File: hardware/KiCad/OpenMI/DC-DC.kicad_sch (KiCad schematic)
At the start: 5 parts

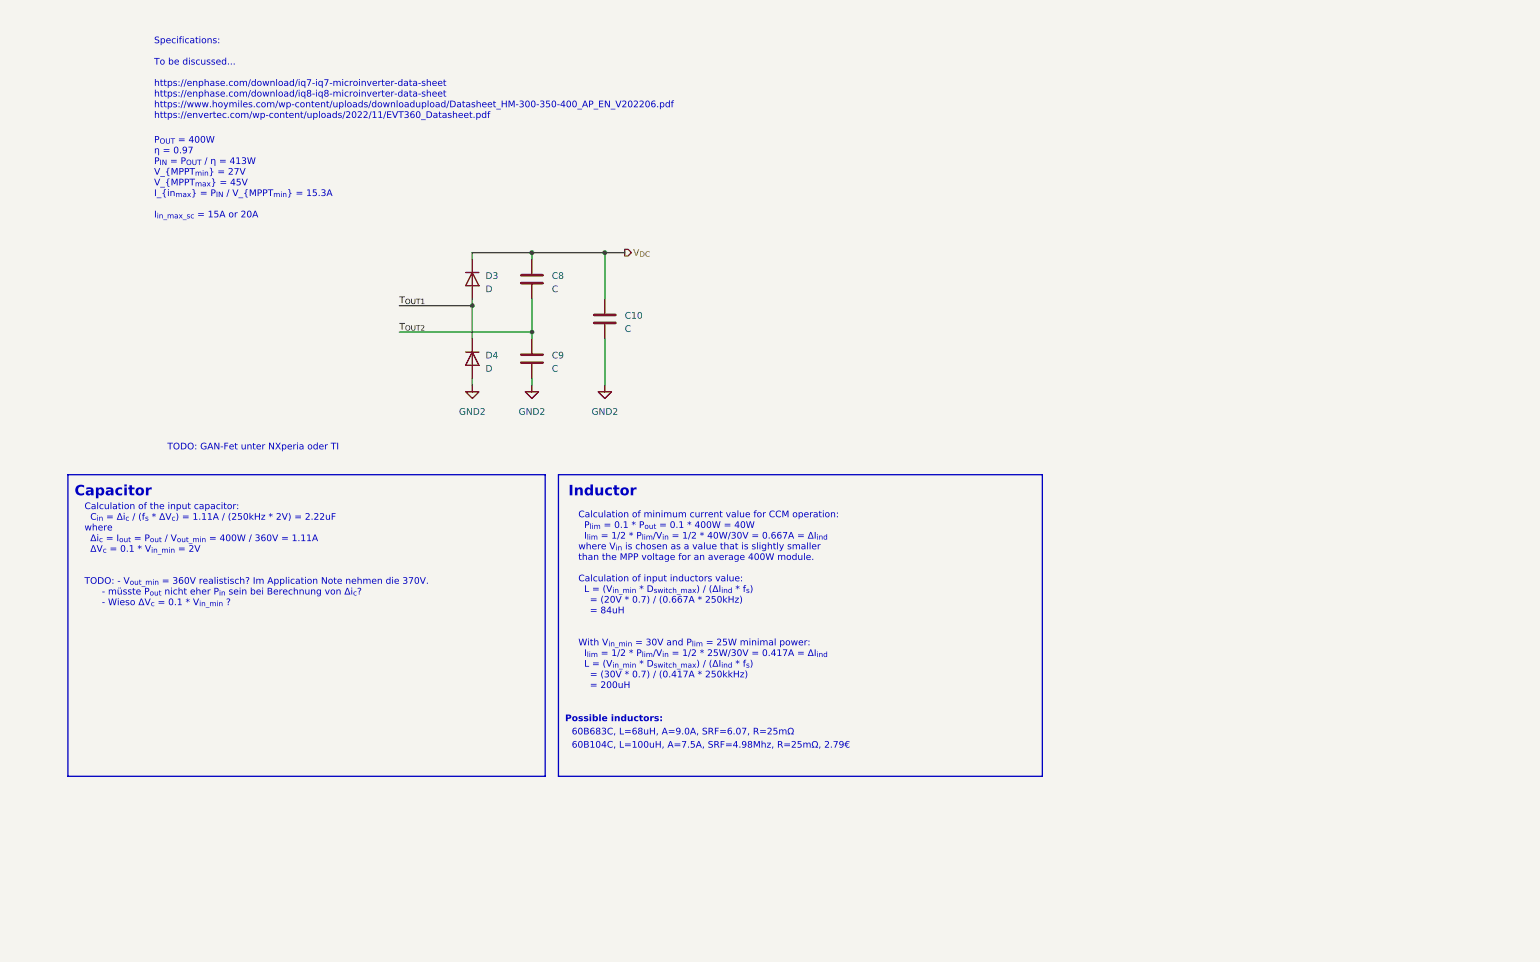
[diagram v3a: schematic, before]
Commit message: feat(hw): Add input capacitance and inductor suggestions
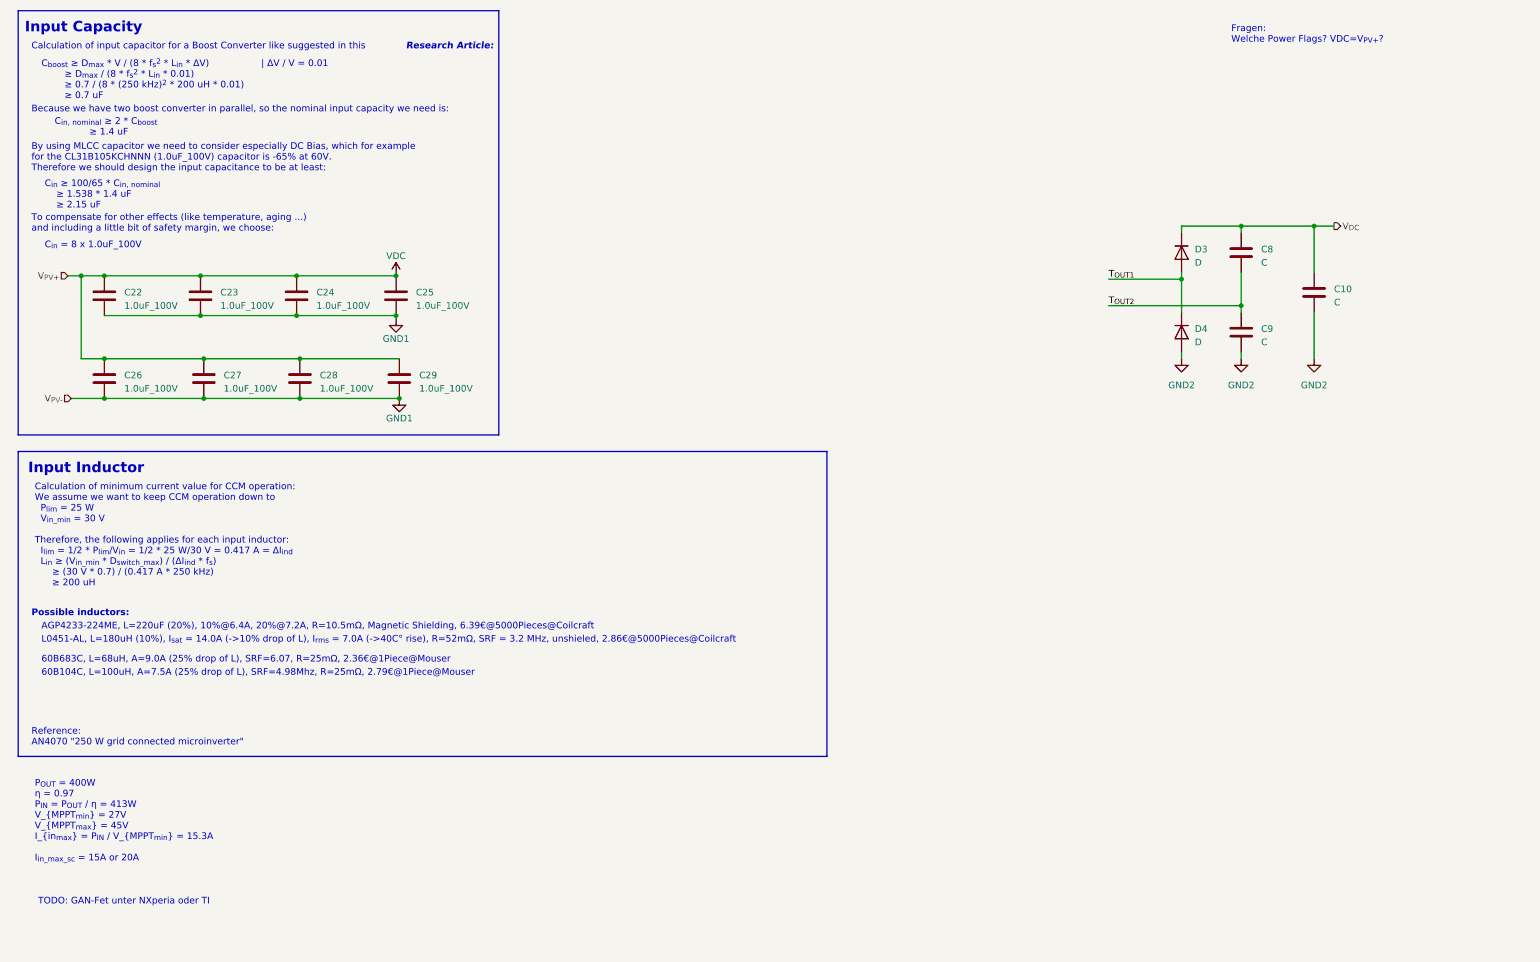
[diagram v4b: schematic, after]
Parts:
- added C22, C23, C24, C25, C26, C27, C28, C29: 1.0uF_100V, Capacitor_SMD:C_1206_3216Metric, symbol _C_1206:1.0uF_100V
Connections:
- new net GND1: C22.2, C23.2, C24.2, C25.2, C26.2, C27.2, C28.2, C29.2
- new net VDC: C22.1, C23.1, C24.1, C25.1, C26.1, C27.1, C28.1, C29.1
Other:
- note added: "60B104C, L=100uH, A=7.5A (25% drop of L), SRF=4.98Mhz, R=25mΩ, 2.79€@1Piece@Mouser"
- note added: "60B683C, L=68uH, A=9.0A (25% drop of L), SRF=6.07, R=25mΩ, 2.36€@1Piece@Mouser"
- note added: "AGP4233-224ME, L=220uF (20%), 10%@6.4A, 20%@7.2A, R=10.5mΩ, Magnetic Shielding, 6.39€@5000Pieces@Coilcraft"
- note added: "Because we have two boost converter in parallel, so the nominal input capacity we need is:"
- note added: "By using MLCC capacitor we need to consider especially DC Bias, which for example for the CL31B105KCHNNN (1.0uF_100V) capacitor is -65% at 60V. Therefore we should design the input capacitance to be at least:"
- note added: "C_{boost} ≥ D_{max} * V / (8 * f_{s}^{2} * L_{in} * ΔV) | ΔV / V = 0.01 ≥ D_{max} / (8 * f_{s}^{2} * L_{in} * 0.01) ≥ 0.7 / (8 * (250 kHz)^{2} * 200 uH * 0.01) ≥ 0.7 uF"
- note added: "C_{in, nominal} ≥ 2 * C_{boost} ≥ 1.4 uF"
- note added: "C_{in} = 8 x 1.0uF_100V"
- note added: "C_{in} ≥ 100/65 * C_{in, nominal} ≥ 1.538 * 1.4 uF ≥ 2.15 uF"
- note added: "Calculation of input capacitor for a Boost Converter like suggested in this"
- note added: "Calculation of minimum current value for CCM operation: We assume we want to keep CCM operation down to P_{lim} = 25 W V_{in_min} = 30 V Therefore, the following applies for each input inductor: I_{lim} = 1/2 * P_{lim}/V_{in} = 1/2 * 25 W/30 V = 0.417 A = ΔI_{ind} L_{in} ≥ (V_{in_min} * D_{switch_max}) / (ΔI_{ind} * f_{s}) ≥ (30 V * 0.7) / (0.417 A * 250 kHz) ≥ 200 uH"
- note added: "Fragen: Welche Power Flags? VDC=V_{PV+}?"
- note added: "Input Capacity"
- note added: "Input Inductor"
- note added: "L0451-AL, L=180uH (10%), I_{sat} = 14.0A (->10% drop of L), I_{rms} = 7.0A (->40C° rise), R=52mΩ, SRF = 3.2 MHz, unshieled, 2.86€@5000Pieces@Coilcraft"
- note added: "Reference: AN4070 "250 W grid connected microinverter""
- note added: "Research Article:"
- note added: "To compensate for other effects (like temperature, aging ...) and including a little bit of safety margin, we choose:"
- note removed: "60B104C, L=100uH, A=7.5A, SRF=4.98Mhz, R=25mΩ, 2.79€"
- note removed: "60B683C, L=68uH, A=9.0A, SRF=6.07, R=25mΩ"
- note removed: "Calculation of minimum current value for CCM operation: P_{lim} = 0.1 * P_{out} = 0.1 * 400W = 40W I_{lim} = 1/2 * P_{lim}/V_{in} = 1/2 * 40W/30V = 0.667A = ΔI_{ind} where V_{in} is chosen as a value that is slightly smaller than the MPP voltage for an average 400W module. Calculation of input inductors value: L = (V_{in_min} * D_{switch_max}) / (ΔI_{ind} * f_{s}) = (20V * 0.7) / (0.667A * 250kHz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"
- note removed: "Calculation of the input capacitor: C_{in} = Δi_{c} / (f_{s} * ΔV_{c}) = 1.11A / (250kHz * 2V) = 2.22uF where Δi_{c} = I_{out} = P_{out} / V_{out_min} = 400W / 360V = 1.11A ΔV_{c} = 0.1 * V_{in_min} = 2V TODO: - V_{out_min} = 360V realistisch? Im Application Note nehmen die 370V. - müsste P_{out} nicht eher P_{in} sein bei Berechnung von Δi_{c}? - Wieso ΔV_{c} = 0.1 * V_{in_min} ?"
- note removed: "Capacitor"
- note removed: "Inductor"
- note removed: "Specifications: To be discussed... https://enphase.com/download/iq7-iq7-microinverter-data-sheet https://enphase.com/download/iq8-iq8-microinverter-data-sheet https://www.hoymiles.com/wp-content/uploads/downloadupload/Datasheet_HM-300-350-400_AP_EN_V202206.pdf https://envertec.com/wp-content/uploads/2022/11/EVT360_Datasheet.pdf"
- moved on the sheet: C10, C8, C9, D3, D4

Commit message: docs(hw): Add first suggestions for GAN-FET
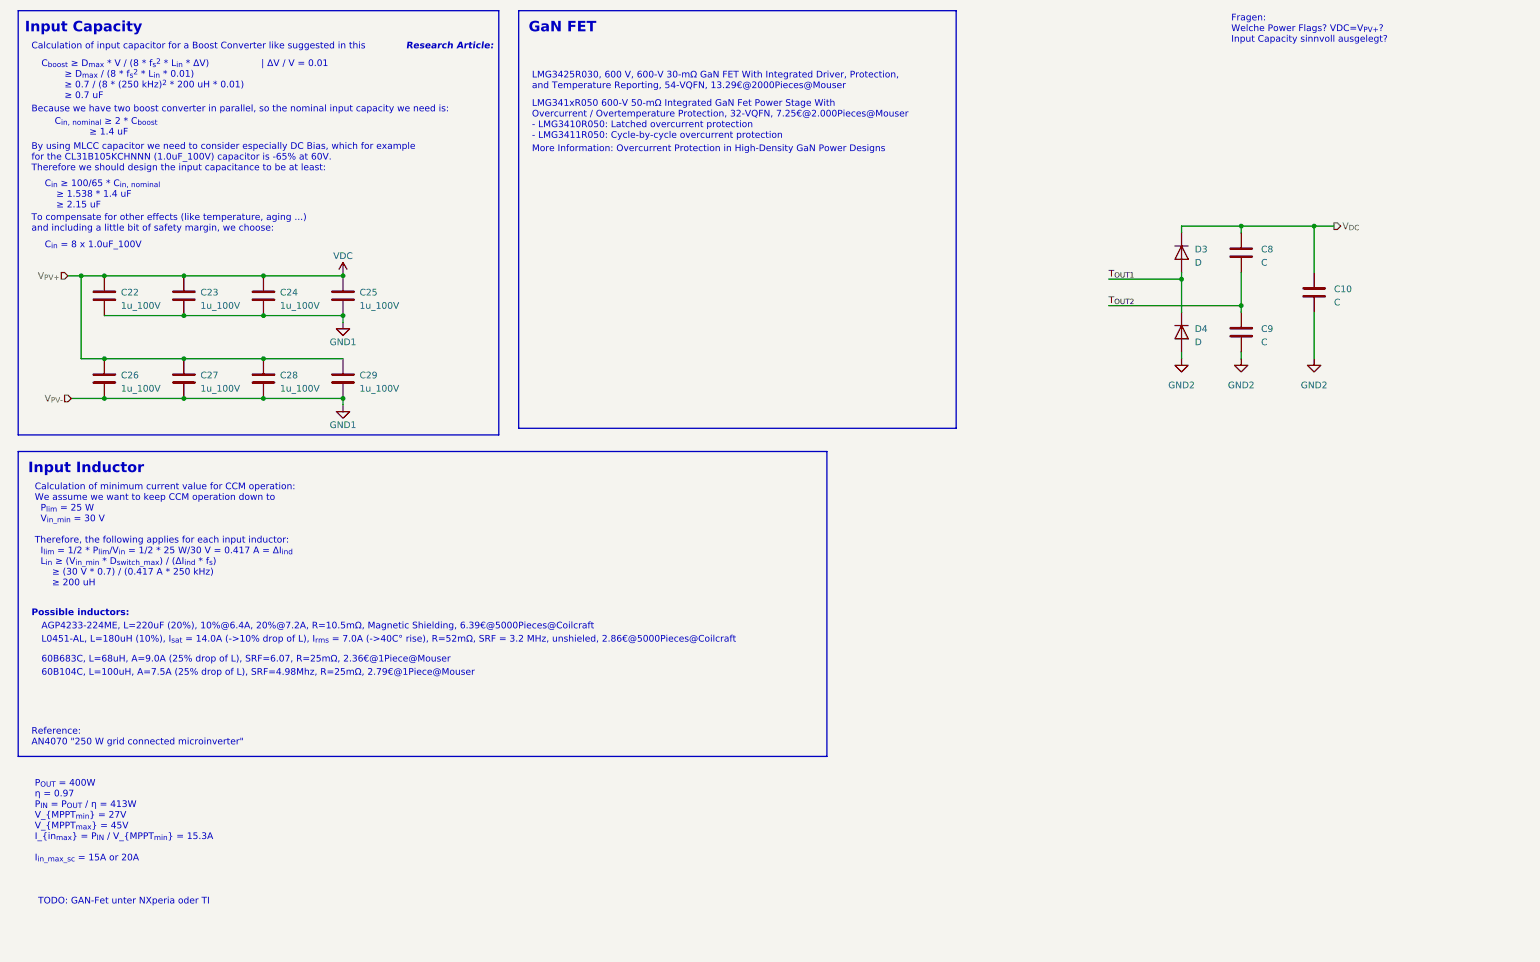
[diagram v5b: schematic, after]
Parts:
- removed C22, C23, C24, C25, C26, C27, C28, C29: 1.0uF_100V, Capacitor_SMD:C_1206_3216Metric, symbol _C_1206:1.0uF_100V
- added C22, C23, C24, C25, C26, C27, C28, C29: 1u_100V, Capacitor_SMD:C_1206_3216Metric, symbol _C_1206:1u_100V
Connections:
- net GND1: now also C22.2, C23.2, C24.2, C25.2, C26.2, C27.2, C28.2, C29.2
- net VDC: now also C22.1, C23.1, C24.1, C25.1, C26.1, C27.1, C28.1, C29.1
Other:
- note added: "Fragen: Welche Power Flags? VDC=V_{PV+}? Input Capacity sinnvoll ausgelegt?"
- note added: "GaN FET"
- note added: "LMG341xR050 600-V 50-mΩ Integrated GaN Fet Power Stage With Overcurrent / Overtemperature Protection, 32-VQFN, 7.25€@2.000Pieces@Mouser - LMG3410R050: Latched overcurrent protection - LMG3411R050: Cycle-by-cycle overcurrent protection"
- note added: "LMG3425R030, 600 V, 600-V 30-mΩ GaN FET With Integrated Driver, Protection, and Temperature Reporting, 54-VQFN, 13.29€@2000Pieces@Mouser"
- note added: "More Information: Overcurrent Protection in High-Density GaN Power Designs"
- note removed: "Fragen: Welche Power Flags? VDC=V_{PV+}?"

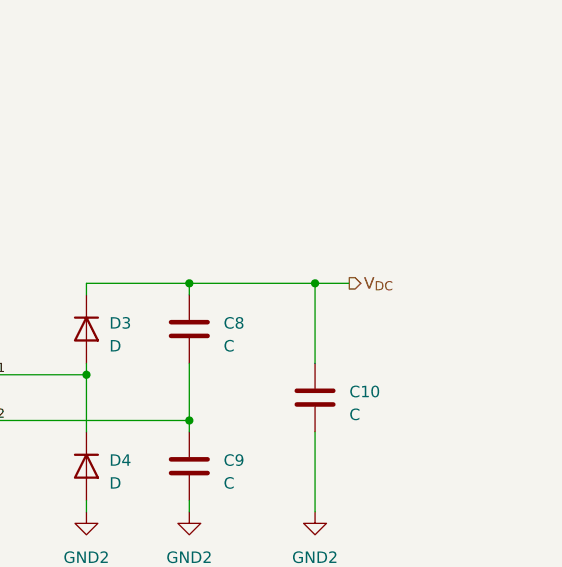
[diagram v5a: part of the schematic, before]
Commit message: refactor(hw): Rename hierarchical label V_DC -> V_BUS
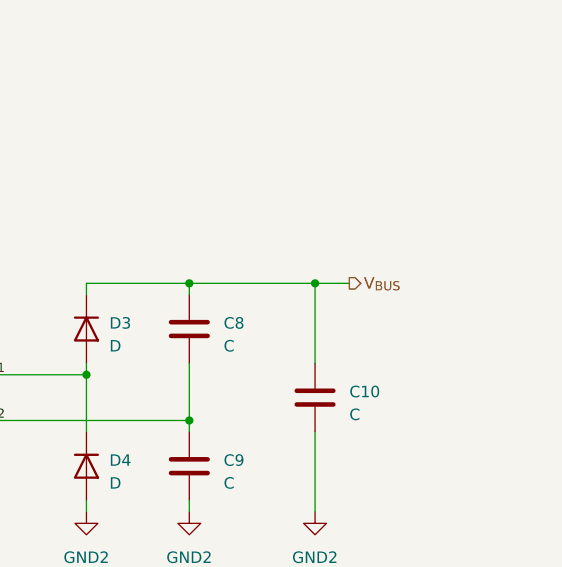
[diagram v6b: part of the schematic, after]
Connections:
- net V_{DC} renamed V_{BUS}
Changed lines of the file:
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@@
     (effects (font (size 1.27 1.27)) (justify left bottom))
   )
-  (hierarchical_label "V_{DC}" (shape output) (at 267.97 57.15 0) (fields_autoplaced)
+  (hierarchical_label "V_{BUS}" (shape output) (at 267.97 57.15 0) (fields_autoplaced)
     (effects (font (size 1.27 1.27)) (justify left))
   )
